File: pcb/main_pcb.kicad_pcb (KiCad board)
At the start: 2 copper layers, 62 x 67 mm, 18 parts, among them J1 Conn_01x06_Socket, SW1 SW_Push, SW2 SW_Push, U1 ESP32-H2-MINI-1, U2 LM5165Y

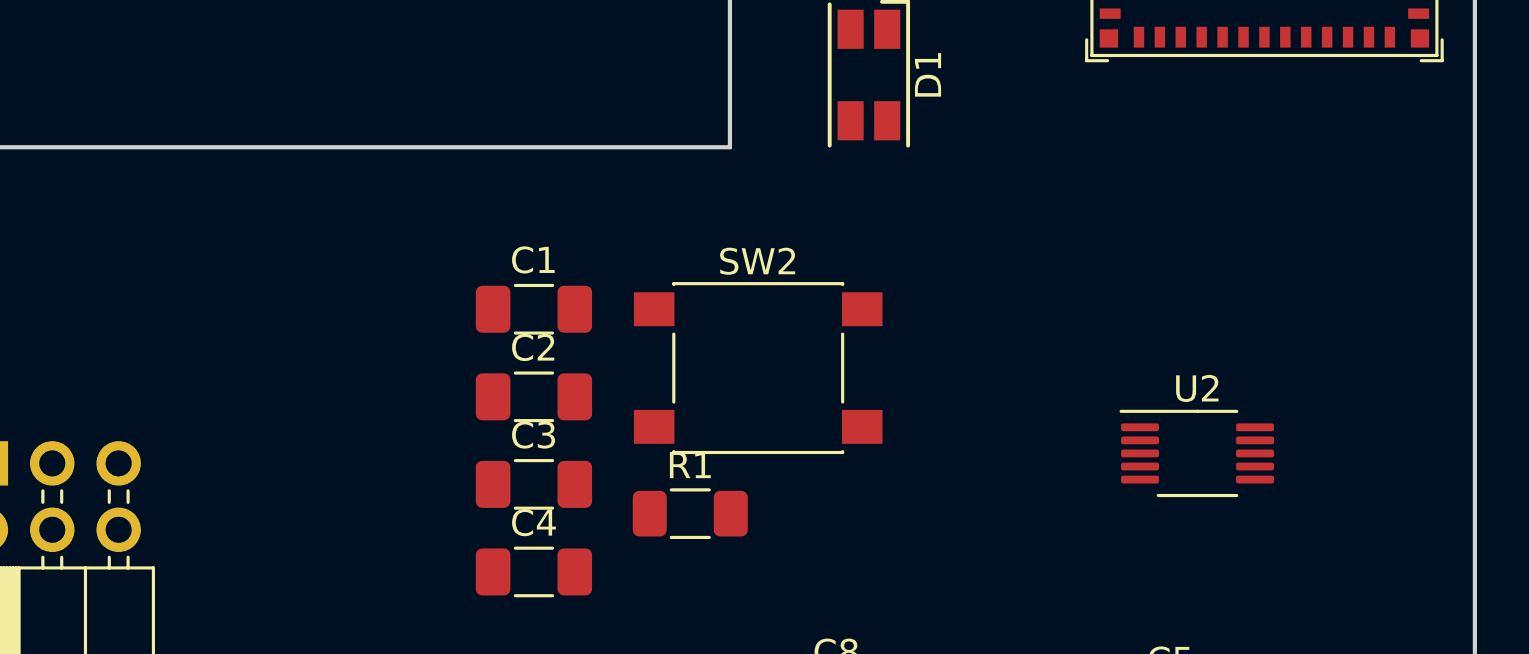
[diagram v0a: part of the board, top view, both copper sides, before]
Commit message: Add JTAG header
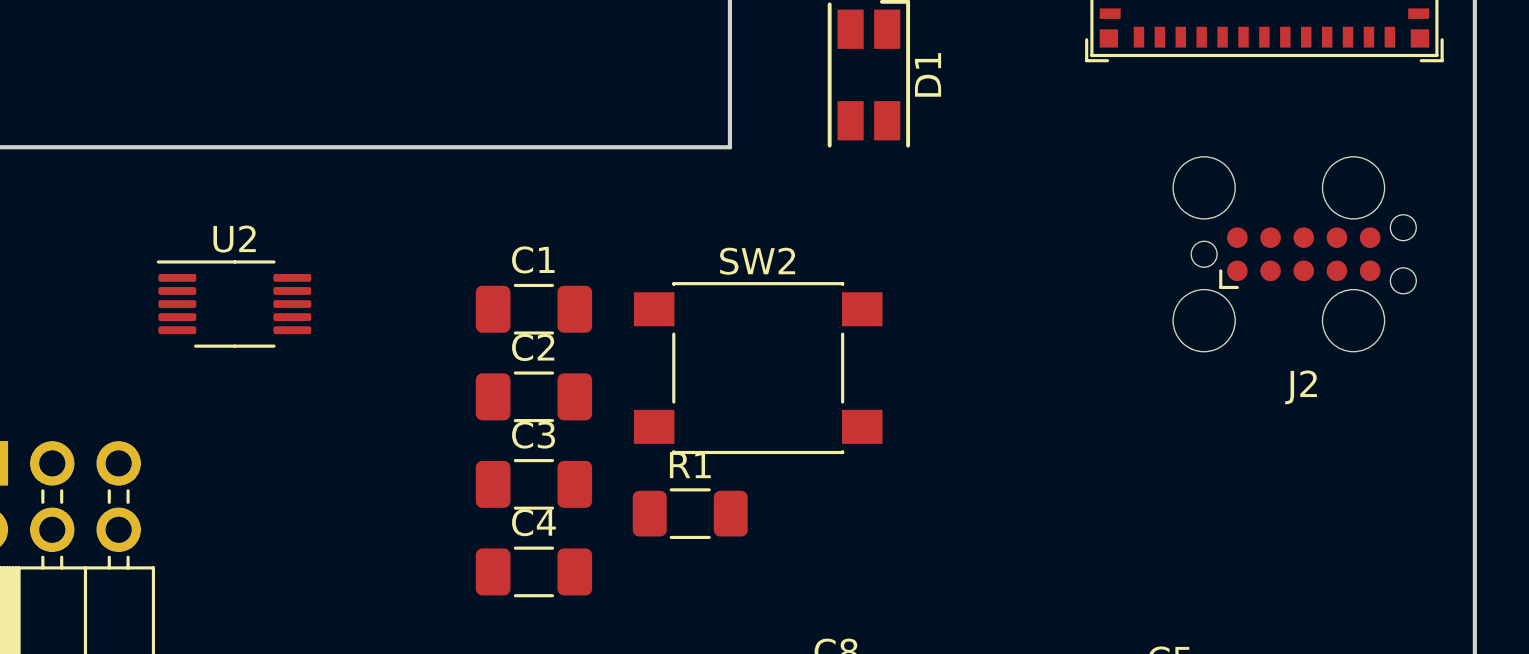
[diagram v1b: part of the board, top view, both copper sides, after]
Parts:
- added J2: Conn_01x10_Pin, Connector:Tag-Connect_TC2050-IDC-FP_2x05_P1.27mm_Vertical, F.Cu at (164.5, 68.3)
- moved U2 37.3 mm to (123.6, 70.2)
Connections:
- U1 pad 18: unconnected-(U1-GPIO4/FSPICLK/ADC1_CH3/MTCK-Pad18) -> /TCK
- U1 pad 19: unconnected-(U1-GPIO5/FSPID/ADC1_CH4/MTDI-Pad19) -> /TDI
- U1 pad 5: unconnected-(U1-GPIO2/FSPIWP/ADC1_CH1/MTMS-Pad5) -> /TMS
- U1 pad 6: unconnected-(U1-GPIO3/FSPIHD/ADC1_CH2/MTDO-Pad6) -> /TDO

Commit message: Add FTDI header
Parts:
- added J3: Conn_01x06_Pin, Connector_PinHeader_2.54mm:PinHeader_1x06_P2.54mm_Horizontal, F.Cu at (120.7, 74.9)
- added JP2: Jumper_2_Open, Connector_PinHeader_2.54mm:PinHeader_1x02_P2.54mm_Horizontal, F.Cu at (137.2, 74.9)
- moved C3 39.4 mm to (158.7, 108.6)
- moved C1 39.4 mm to (158.7, 101.9)
- moved C2 39.4 mm to (158.7, 105.2)
- moved C4 39.4 mm to (158.7, 111.9)
- moved R1 39.4 mm to (164.7, 109.7)
- moved SW2 39.4 mm to (167.3, 104.1)
- moved U2 30.0 mm to (132.0, 99.1)
- moved J1 2.16 mm to (111.9, 76.3)
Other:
- board text added: "FTID"
- board text added: "PWR_EN"

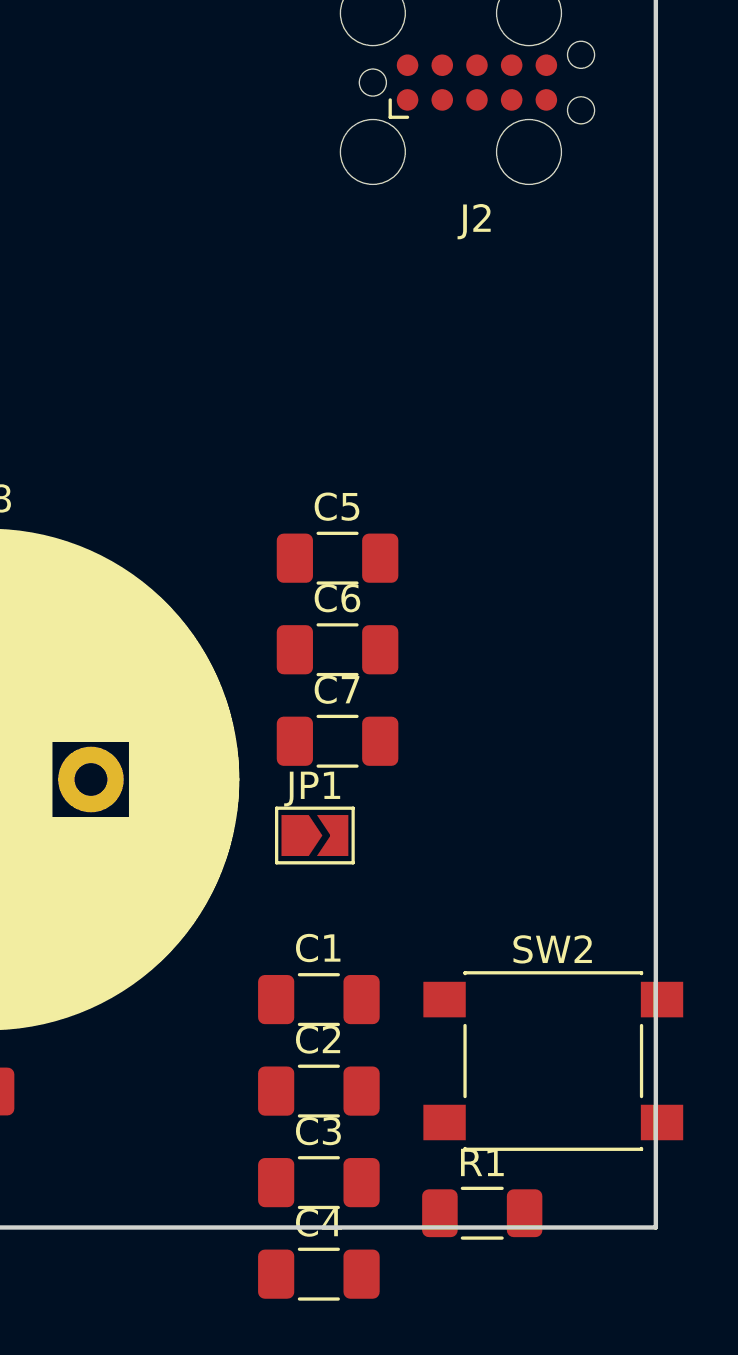
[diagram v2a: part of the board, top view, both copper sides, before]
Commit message: Add optional soft start capacitor to power circuit
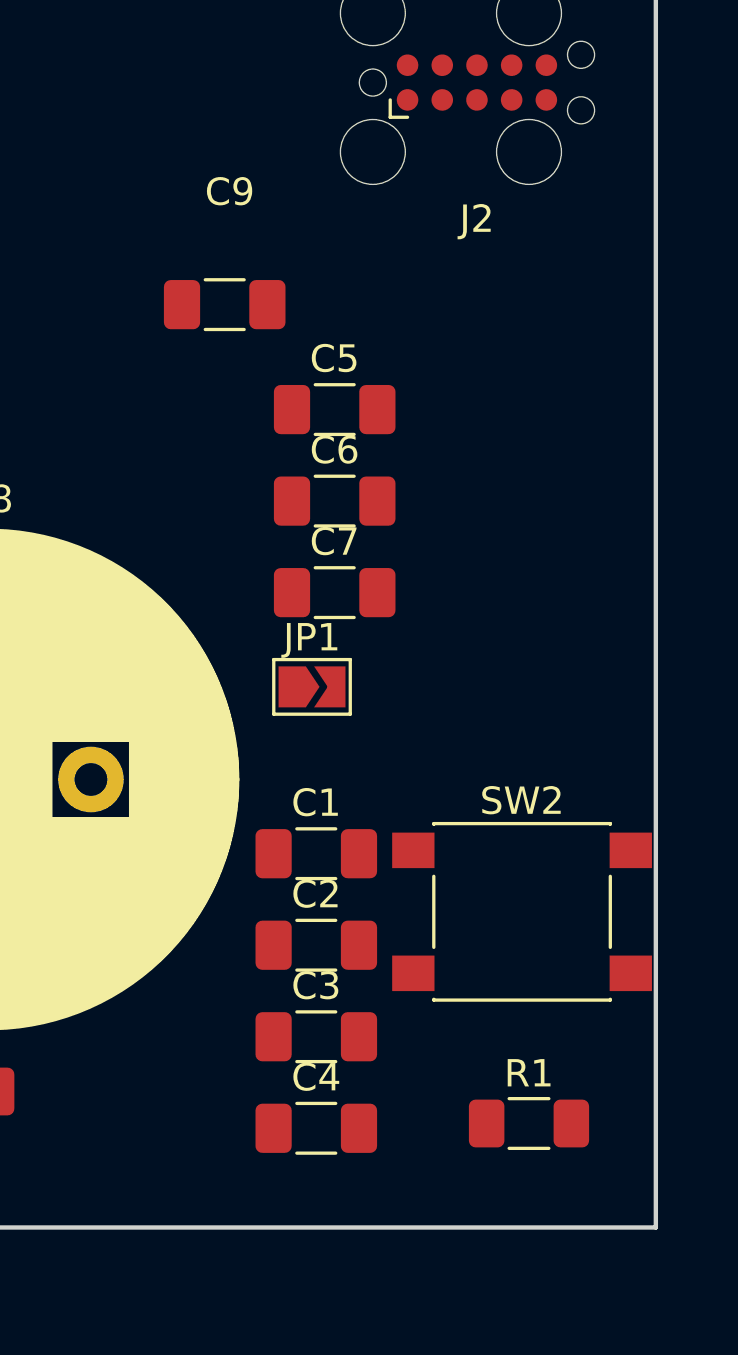
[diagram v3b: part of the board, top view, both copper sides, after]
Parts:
- added C9: 1uF, Capacitor_SMD:C_1206_3216Metric_Pad1.33x1.80mm_HandSolder, F.Cu at (155.2, 76.5)
- moved SW2 5.58 mm to (166.1, 98.7)
- moved JP1 5.44 mm to (158.4, 90.4)
- moved C5 5.44 mm to (159.3, 80.3)
- moved C6 5.44 mm to (159.3, 83.6)
- moved C7 5.44 mm to (159.3, 87.0)
- moved C1 5.34 mm to (158.6, 96.6)
- moved C2 5.34 mm to (158.6, 99.9)
- moved C3 5.34 mm to (158.6, 103.3)
- moved C4 5.34 mm to (158.6, 106.6)
- moved R1 3.70 mm to (166.4, 106.4)
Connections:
- U1 pad 30: unconnected-(U1-GPIO23/FSPICS1/U0RXD-Pad30) -> /TXD
- U1 pad 31: unconnected-(U1-GPIO24/FSPICS2/U0TXD-Pad31) -> /RXD
- U2 pad 4: unconnected-(U2-SS-Pad4) -> Net-(U2-SS)

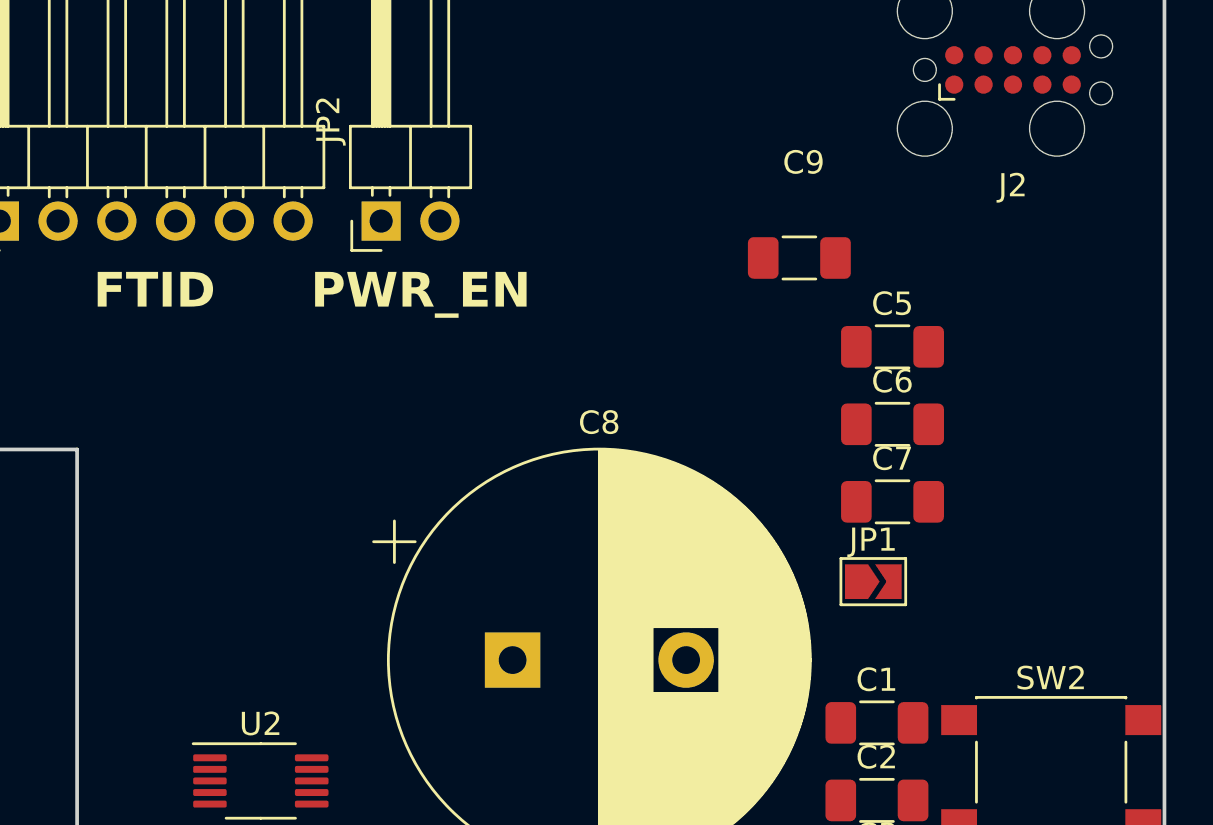
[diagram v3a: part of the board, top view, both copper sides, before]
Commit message: Add USB-C receptacle
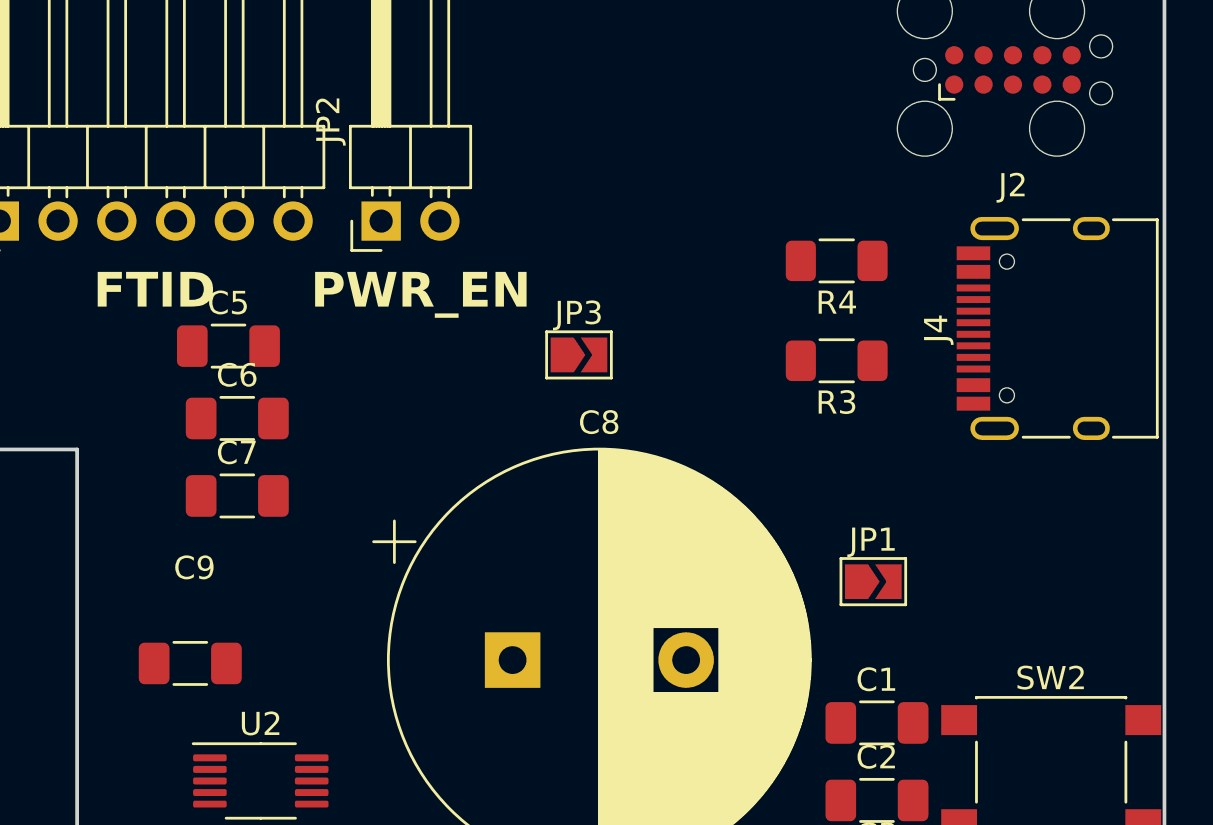
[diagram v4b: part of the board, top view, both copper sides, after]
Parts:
- added J4: USB_C_Receptacle_USB2.0, Connector_USB:USB_C_Receptacle_HRO_TYPE-C-31-M-12, F.Cu at (166.8, 79.5)
- added JP3: SolderJumper_2_Bridged, Jumper:SolderJumper-2_P1.3mm_Open_TrianglePad1.0x1.5mm, F.Cu at (145.7, 80.6)
- added R3: 5k1, Resistor_SMD:R_1206_3216Metric_Pad1.30x1.75mm_HandSolder, F.Cu at (156.8, 80.9)
- added R4: 5k1, Resistor_SMD:R_1206_3216Metric_Pad1.30x1.75mm_HandSolder, F.Cu at (156.8, 76.6)
- moved C9 31.6 mm to (128.9, 94.0)
- moved C5 28.7 mm to (130.6, 80.3)
- moved C6 28.3 mm to (130.9, 83.4)
- moved C7 28.3 mm to (130.9, 86.7)
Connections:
- U1 pad 26: unconnected-(U1-GPIO26/FSPICS4/USB_D--Pad26) -> /D-
- U1 pad 27: unconnected-(U1-GPIO27/FSPICS5/USB_D+-Pad27) -> /D+

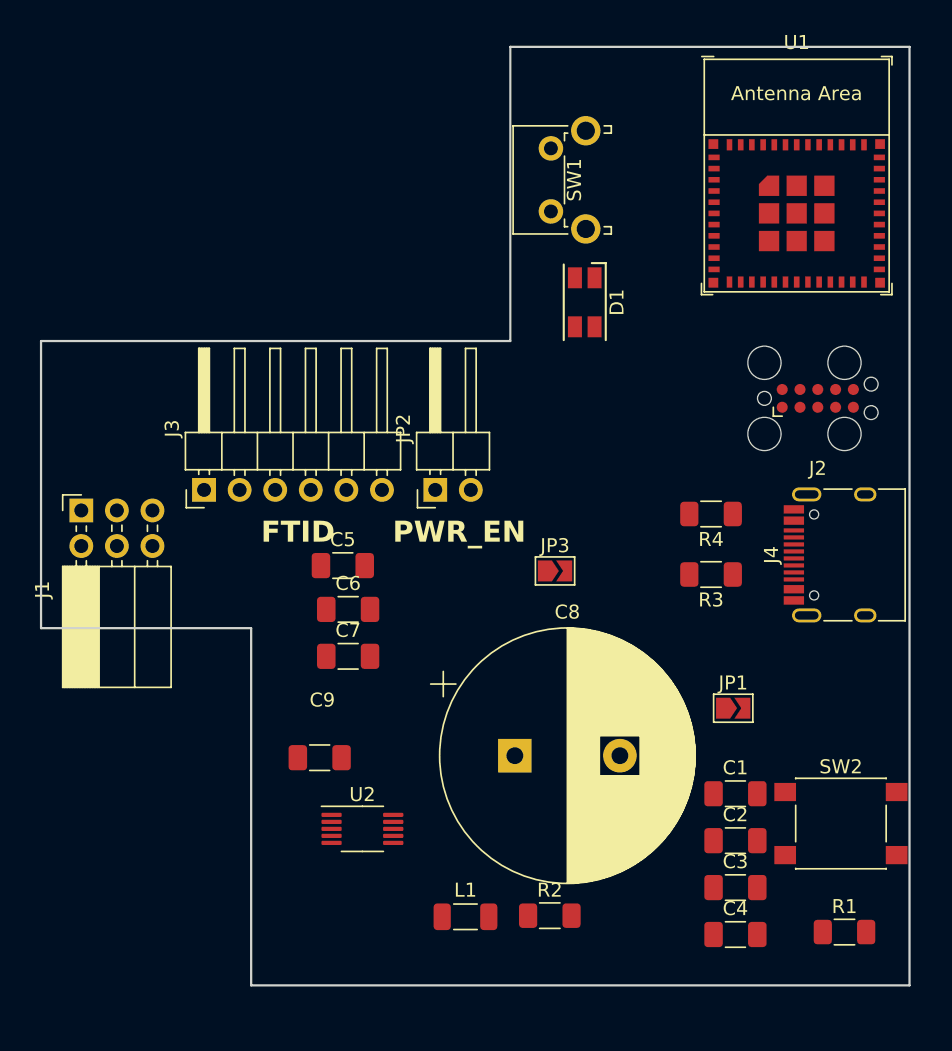
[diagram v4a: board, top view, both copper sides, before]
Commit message: Add boot selection circuit
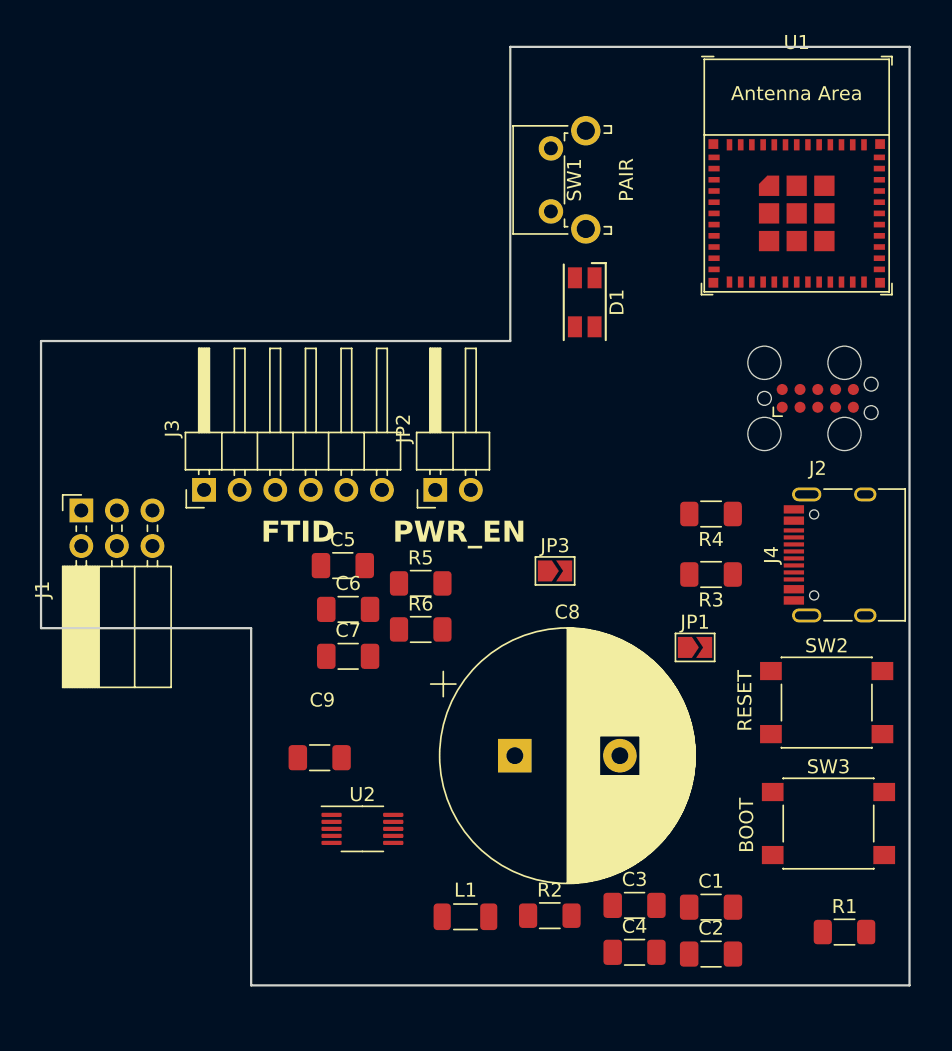
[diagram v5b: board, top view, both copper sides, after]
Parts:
- added R5: 10k, Resistor_SMD:R_1206_3216Metric_Pad1.30x1.75mm_HandSolder, F.Cu at (136.1, 81.5)
- added R6: 10k, Resistor_SMD:R_1206_3216Metric_Pad1.30x1.75mm_HandSolder, F.Cu at (136.1, 84.8)
- added SW3: BOOT, Button_Switch_SMD:SW_SPST_PTS645, F.Cu at (165.2, 98.7)
- SW1: value SW_Push -> PAIR
- SW2: value SW_Push -> RESET
- moved SW2 8.70 mm to (165.1, 90.0)
- moved C2 8.28 mm to (156.8, 108.0)
- moved C1 8.28 mm to (156.8, 104.6)
- moved C3 7.31 mm to (151.4, 104.5)
- moved C4 7.31 mm to (151.4, 107.9)
- moved JP1 5.12 mm to (155.7, 86.1)
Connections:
- U1 pad 16: unconnected-(U1-GPIO12-Pad16) -> Net-(U1-GPIO12)
- U1 pad 22: unconnected-(U1-GPIO8-Pad22) -> Net-(U1-GPIO8)
